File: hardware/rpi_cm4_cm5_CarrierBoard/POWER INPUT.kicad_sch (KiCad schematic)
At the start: 18 parts, among them J15 694106301002, Q1 DMPH6050SK3-13, U36 INA180A2IDBVR

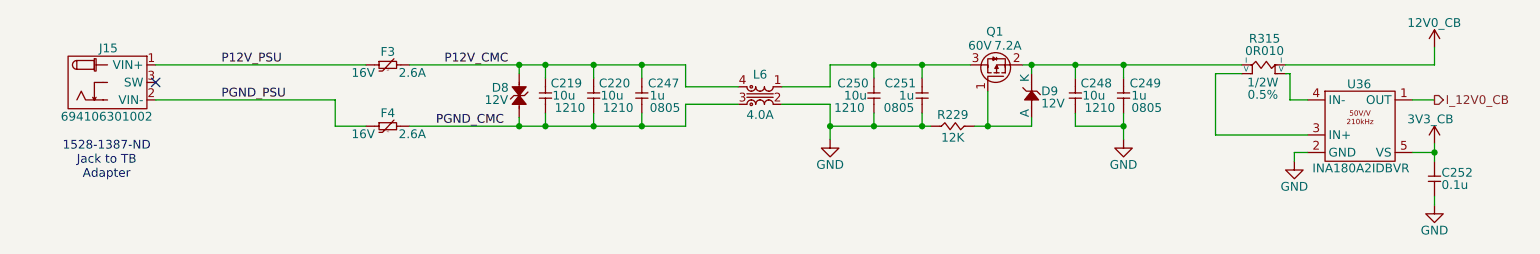
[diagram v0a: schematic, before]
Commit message: Update watchdog timer circuit to add external watchdog timer IC to be fed by PIC Adjust reset scheme in power supply sheet accordingly Adjust PinMux, regen BOM and PDF schematics (preliminary) Start preliminary component placement in the PCB
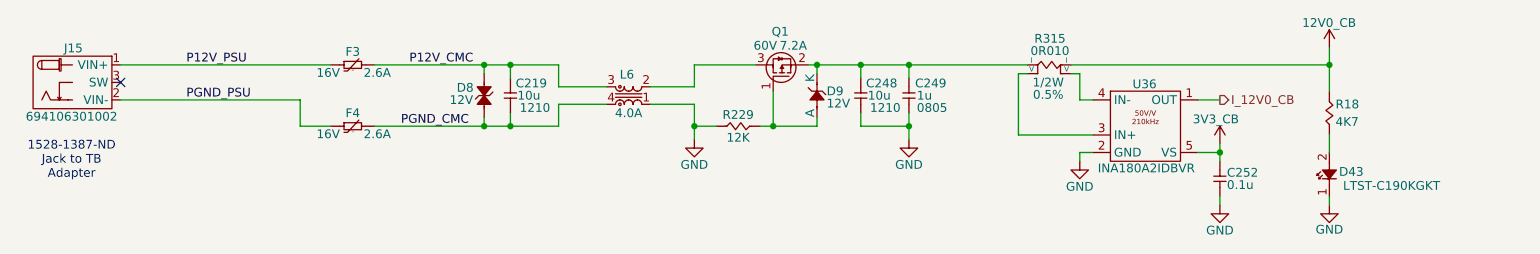
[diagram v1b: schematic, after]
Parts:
- removed C220, C250: 10u, footprint:CAP_NONPOL_1210, symbol KicadCompDb:Capacitors/CAP_CER_SMT_00014
- removed C247, C251: 1u, footprint:CAP_NONPOL_0805, symbol KicadCompDb:Capacitors/CAP_CER_SMT_00002
- added D43: LTST-C190KGKT, footprint:LED_0603, symbol KicadCompDb:Diodes/DIODE_00007
- added R18: 4K7, footprint:RES_0402, symbol KicadCompDb:Resistors/RES_SMT_00010
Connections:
- net 12V0_CB: now also R18.2
- net GND: now also L6.1, D43.1 (K); no longer L6.2
- net P12V_CMC: now also L6.3; no longer L6.4
- net PGND_CMC: now also L6.4; no longer L6.3
- net at Q1.3 (D): now also L6.2; no longer L6.1
- new net: D43.2 (A), R18.1
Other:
- moved on the sheet: C219, C248, C249, C252, D8, D9, F3, F4, J15, L6, Q1, R229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

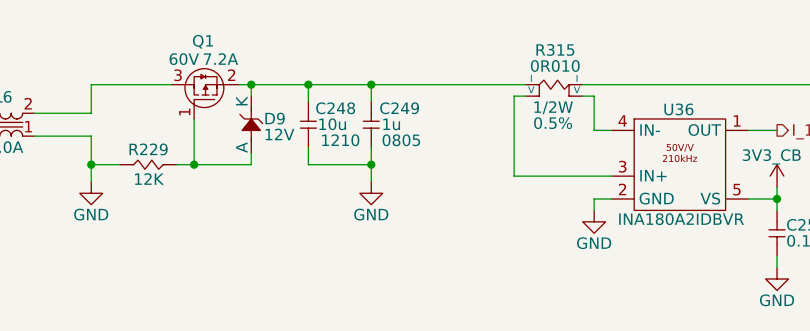
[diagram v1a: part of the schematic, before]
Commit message: Update PCB design rules for outer layers differential pairs Update preliminary component placement Update schematics based on PCB placement & remove duplicata / unnecessary components Update design notes and power table
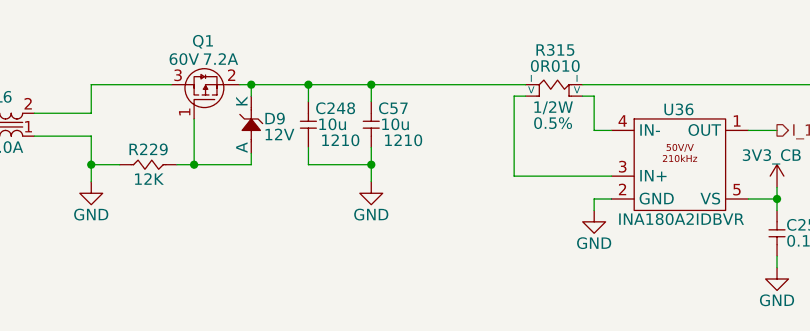
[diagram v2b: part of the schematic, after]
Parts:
- removed C249: 1u, footprint:CAP_NONPOL_0805, symbol KicadCompDb:Capacitors/CAP_CER_SMT_00002
- added C57: 10u, footprint:CAP_NONPOL_1210, symbol KicadCompDb:Capacitors/CAP_CER_SMT_00014
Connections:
- net GND: now also C57.1
- net at C248.2, D9.1 (K), Q1.2 (S)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: now also C57.2
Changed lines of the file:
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@@
-	)
-	(symbol
-		(lib_id "KicadCompDb:Capacitors/CAP_CER_SMT_00002")
-		(at 173.99 93.98 90)
-		(unit 1)
-		(exclude_from_sim no)
-		(in_bom yes)
-		(on_board yes)
-		(dnp no)
-		(property "Reference" "C249"
-			(at 174.879 89.662 90)
-			(effects
-				(font
-					(size 1.27 1.27)
-				)
-				(justify right)
-			)
-		)
-		(property "Value" "1u"
-			(at 175.133 91.44 90)
-			(effects
-				(font
-					(size 1.27 1.27)
-				)
-				(justify right)
-			)
-		)
-		(property "Footprint" "footprint:CAP_NONPOL_0805"
-			(at 196.088 93.472 0)
-			(effects
-				(font
-					(size 1.27 1.27)
-				)
-				(hide yes)
-			)
-		)
-		(property "Datasheet" "https://www.yageogroup.com/content/datasheet/asset/file/UPY-GPHC_X7R_6_3V-TO-250V"
-			(at 173.99 93.98 0)
-			(effects
-				(font
-					(size 1.27 1.27)
-				)
-				(hide yes)
-			)
-		)
-		(property "Description" "CAP CER 1UF 50V X7R 0805"
-			(at 183.896 92.202 0)
-			(effects
-				(font
-					(size 1.27 1.27)
-				)
-				(hide yes)
-			)
-		)
-		(property "Tolerance" "±10%"
-			(at 194.31 93.726 0)
-			(effects
-				(font
-					(size 1.27 1.27)
-				)
-				(hide yes)
-			)
-		)
-		(property "Dielectric" "X7R"
-			(at 188.214 93.726 0)
-			(effects
-				(font
-					(size 1.27 1.27)
-				)
-				(hide yes)
-			)
-		)
-		(property "Package" "0805"
-			(at 175.133 93.218 90)
-			(effects
-				(font
-					(size 1.27 1.27)
-				)
-				(justify right)
-			)
-		)
-		(property "Operating Temperature" "-55°C ~ 125°C"
-			(at 198.374 93.218 0)
-			(effects
-				(font
-					(size 1.27 1.27)
-				)
-				(hide yes)
-			)
-		)
-		(property "Voltage Rating" "50V"
-			(at 175.006 92.583 90)
-			(effects
-				(font
-					(size 1.27 1.27)
-				)
-				(justify right)
-				(hide yes)
-			)
-		)
-		(property "Manufacturer" "YAGEO"
-			(at 192.278 93.726 0)
-			(effects
-				(font
-					(size 1.27 1.27)
-				)
-				(hide yes)
-			)
-		)
-		(property "Manufacturer Part Number" "CC0805KKX7R9BB105"
-			(at 181.864 93.726 0)
-			(effects
-				(font
-					(size 1.27 1.27)
-				)
-				(hide yes)
-			)
-		)
-		(property "Distributor" "DigiKey"
-			(at 179.832 93.98 0)
-			(effects
-				(font
-					(size 1.27 1.27)
-				)
-				(hide yes)
-			)
-		)
-		(property "Distributor Part Number" "311-1886-1-ND"
-			(at 186.182 93.218 0)
-			(effects
-				(font
-					(size 1.27 1.27)
-				)
-				(hide yes)
-			)
-		)
-		(property "Type" "CER SMT"
-			(at 173.99 93.98 0)
-			(show_name yes)
-			(effects
-				(font
-					(size 1.27 1.27)
-				)
-				(hide yes)
-			)
-		)
-		(property "Dimensions" "2.00mm x 1.25mm"
-			(at 173.99 93.98 0)
-			(show_name yes)
-			(effects
-				(font
-					(size 1.27 1.27)
-				)
-				(hide yes)
-			)
-		)
-		(pin "1"
-		)
-		(pin "2"
-		)
-		(instances
-			(project "rpi_cm4_cm5_CarrierBoard"
-				(path "/7dcdf741-90ca-4333-848c-806f4d64158e/5b092eaf-fa47-43ab-9b96-d2aeda0b5528"
-					(reference "C249")
-					(unit 1)
-				)
-			)
-		)
 	)
 	(symbol
@@
 					(unit 1)
 				)
+			)
+		)
+	)
+	(symbol
+		(lib_id "KicadCompDb:Capacitors/CAP_CER_SMT_00014")
+		(at 173.99 93.98 90)
+		(unit 1)
+		(exclude_from_sim no)
+		(in_bom yes)
+		(on_board yes)
+		(dnp no)
+		(property "Reference" "C57"
+			(at 174.752 89.662 90)
+			(effects
+				(font
+					(size 1.27 1.27)
+				)
+				(justify right)
+			)
+		)
+		(property "Value" "10u"
+			(at 175.006 91.44 90)
+			(effects
+				(font
+					(size 1.27 1.27)
+				)
+				(justify right)
+			)
+		)
+		(property "Footprint" "footprint:CAP_NONPOL_1210"
+			(at 196.088 93.472 0)
+			(effects
+				(font
+					(size 1.27 1.27)
+				)
+				(hide yes)
+			)
+		)
+		(property "Datasheet" "https://product.tdk.com/system/files/dam/doc/product/capacitor/ceramic/mlcc/charasheet/c3225x7r1h106k250ac_200131.pdf"
+			(at 173.99 93.98 0)
+			(effects
+				(font
+					(size 1.27 1.27)
+				)
+				(hide yes)
+			)
+		)
+		(property "Description" "CAP CER 10UF 50V X7R 1210"
+			(at 183.896 92.202 0)
+			(effects
+				(font
+					(size 1.27 1.27)
+				)
+				(hide yes)
+			)
+		)
+		(property "Tolerance" "±10%"
+			(at 194.31 93.726 0)
+			(effects
+				(font
+					(size 1.27 1.27)
+				)
+				(hide yes)
+			)
+		)
+		(property "Dielectric" "X7R"
+			(at 188.214 93.726 0)
+			(effects
+				(font
+					(size 1.27 1.27)
+				)
+				(hide yes)
+			)
+		)
+		(property "Package" "1210"
+			(at 177.546 93.218 90)
+			(effects
+				(font
+					(size 1.27 1.27)
+				)
+			)
+		)
+		(property "Operating Temperature" "-55°C ~ 125°C"
+			(at 198.374 93.218 0)
+			(effects
+				(font
+					(size 1.27 1.27)
+				)
+				(hide yes)
+			)
+		)
+		(property "Voltage Rating" "50V"
+			(at 173.99 93.98 0)
+			(effects
+				(font
+					(size 1.27 1.27)
+				)
+				(hide yes)
+			)
+		)
+		(property "Manufacturer" "TDK Corporation"
+			(at 192.278 93.726 0)
+			(effects
+				(font
+					(size 1.27 1.27)
+				)
+				(hide yes)
+			)
+		)
+		(property "Manufacturer Part Number" "C3225X7R1H106K250AC"
+			(at 181.864 93.726 0)
+			(effects
+				(font
+					(size 1.27 1.27)
+				)
+				(hide yes)
+			)
+		)
+		(property "Distributor" "DigiKey"
+			(at 179.832 93.98 0)
+			(effects
+				(font
+					(size 1.27 1.27)
+				)
+				(hide yes)
+			)
+		)
+		(property "Distributor Part Number" "445-C3225X7R1H106K250ACCT-ND"
+			(at 186.182 93.218 0)
+			(effects
+				(font
+					(size 1.27 1.27)
+				)
+				(hide yes)
+			)
+		)
+		(property "Type" "CER SMT"
+			(at 173.99 93.98 0)
+			(show_name yes)
+			(effects
+				(font
+					(size 1.27 1.27)
+				)
+				(hide yes)
+			)
+		)
+		(property "Dimensions" "3.20mm x 2.50mm"
+			(at 173.99 93.98 0)
+			(show_name yes)
+			(effects
+				(font
+					(size 1.27 1.27)
+				)
+				(hide yes)
+			)
+		)
+		(pin "1"
+		)
+		(pin "2"
+		)
+		(instances
+			(project "rpi_cm4_cm5_CarrierBoard"
+				(path "/7dcdf741-90ca-4333-848c-806f4d64158e/5b092eaf-fa47-43ab-9b96-d2aeda0b5528"
+					(reference "C57")
+					(unit 1)
+				)
